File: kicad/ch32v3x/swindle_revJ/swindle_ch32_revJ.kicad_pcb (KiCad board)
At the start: 2 copper layers, 49.8 x 33.3 mm, 64 parts, among them J1 jtag, J2 Conn_01x03_Socket, J2_DFU1 con2, J3 Dbg, J4 USB, J5 Debug port, U1 CH32V303RCT6, U2 LM1117-3.3, U3 3V->VTREF, U4 VTREF->3V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

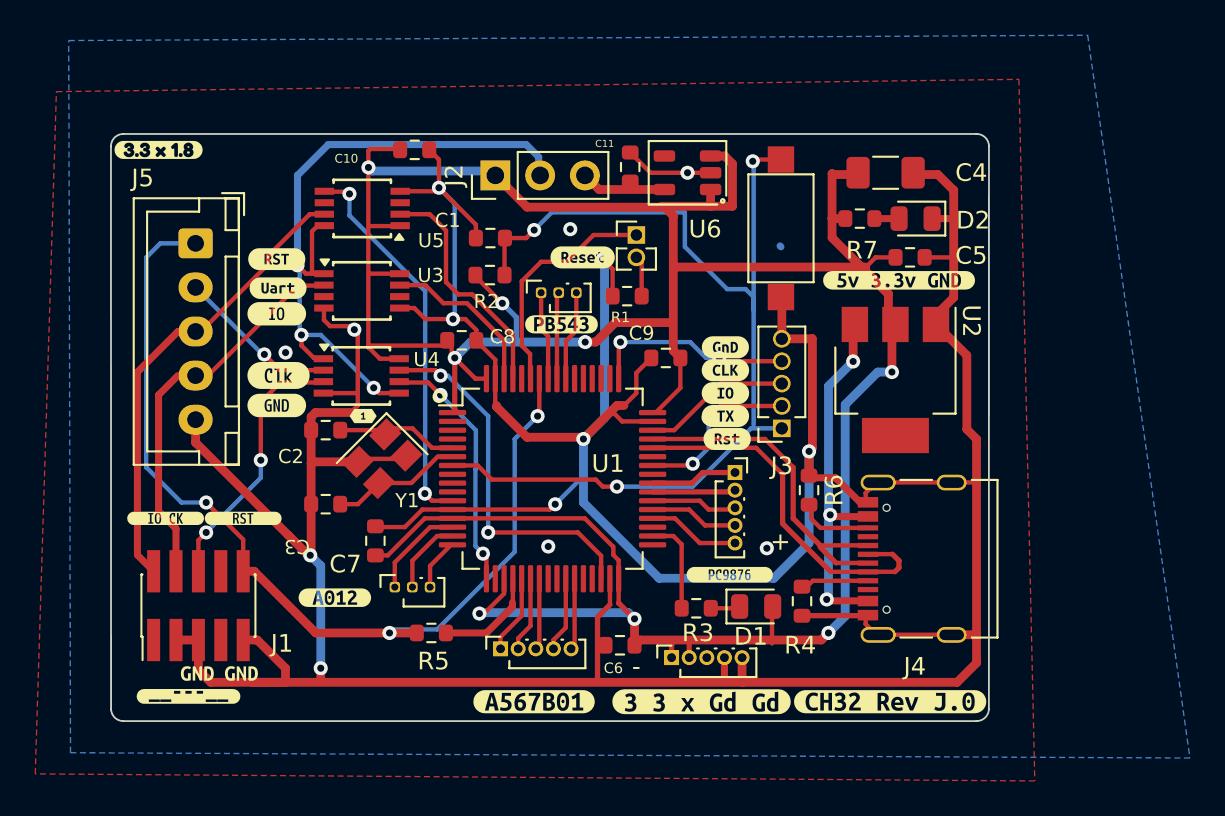
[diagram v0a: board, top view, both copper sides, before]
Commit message: update CH32 pcb
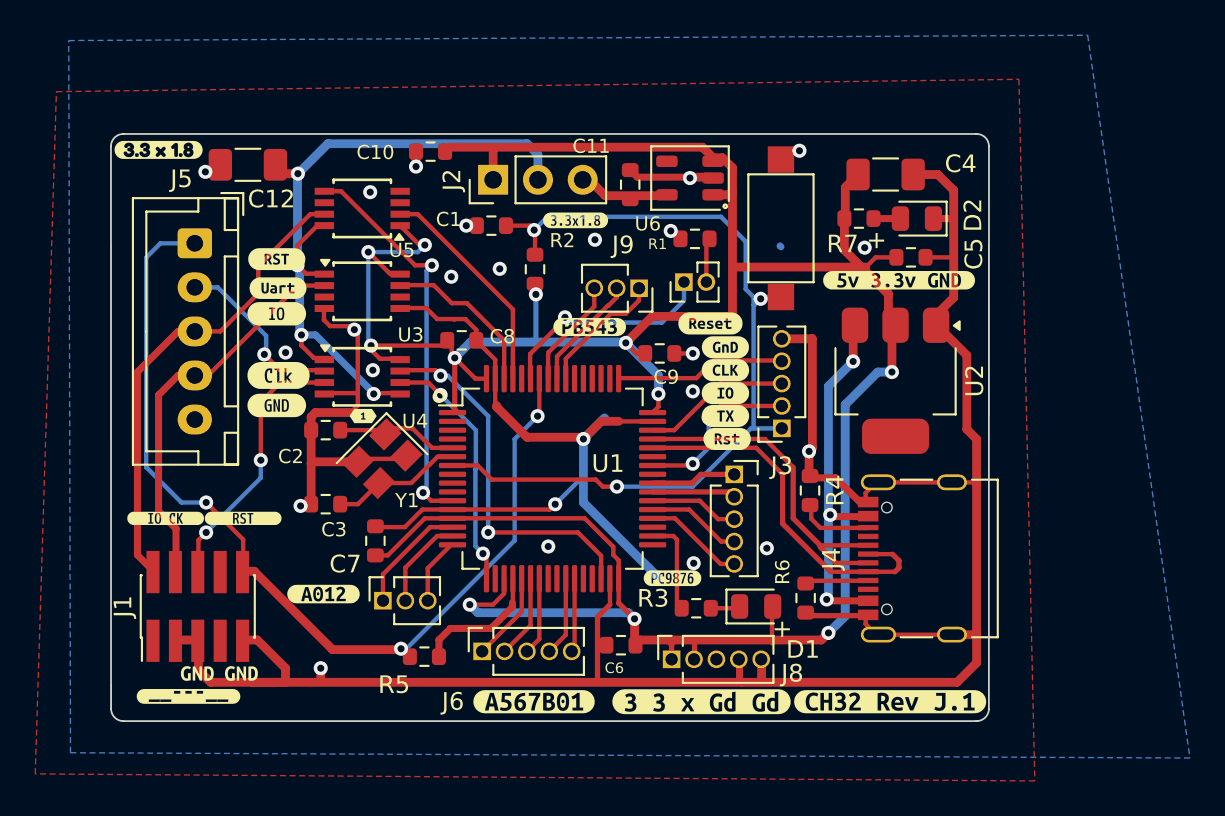
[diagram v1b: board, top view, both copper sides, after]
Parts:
- removed -, PA4567, x2: PinSocket_1x05_P1.00mm_Vertical, Connector_PinSocket_1.00mm:PinSocket_1x05_P1.00mm_Vertical
- removed PB567: PIN1X3, Connector_PinSocket_1.00mm:PinSocket_1x03_P1.00mm_Vertical
- removed kibuzzard-6713D043: G***, kibuzzard-6713D043
- removed kibuzzard-68455F40: G***, kibuzzard-68455F40
- removed x: PinSocket_1x03_P1.00mm_Vertical, Connector_PinSocket_1.00mm:PinSocket_1x03_P1.00mm_Vertical
- added C12: 100u, Capacitor_SMD:C_1206_3216Metric_Pad1.33x1.80mm_HandSolder, F.Cu at (113.3, 68.6)
- added J10: Debug port, Connector_PinSocket_1.27mm:PinSocket_1x05_P1.27mm_Vertical, F.Cu at (140.9, 86.2)
- added J6: Debug port, Connector_PinSocket_1.27mm:PinSocket_1x05_P1.27mm_Vertical, F.Cu at (126.6, 96.2)
- added J7: Conn_01x03_Pin, Connector_PinSocket_1.27mm:PinSocket_1x03_P1.27mm_Vertical, F.Cu at (120.9, 93.4)
- added J8: Debug port, Connector_PinSocket_1.27mm:PinSocket_1x05_P1.27mm_Vertical, F.Cu at (137.3, 96.7)
- added J9: Conn_01x03_Pin, Connector_PinSocket_1.27mm:PinSocket_1x03_P1.27mm_Vertical, F.Cu at (135.5, 75.6)
- added kibuzzard-6869421E: G***, kibuzzard-6869421E, F.Cu at (149.7, 99.1)
- added kibuzzard-68694355: G***, kibuzzard-68694355, F.Cu at (137.4, 92.1)
- added kibuzzard-686943DA: G***, kibuzzard-686943DA, F.Cu at (131.9, 71.8)
- moved kibuzzard-65C1C9D7 8.16 mm to (139.5, 77.6)
- moved R4 6.30 mm to (145.2, 87.1), turned to -90 degrees
- moved R6 6.12 mm to (144.9, 93.2), turned to 90 degrees
- moved R1 5.04 mm to (138.6, 72.8)
- moved J2_DFU1 3.80 mm to (138.0, 75.3), turned to 90 degrees
- moved R2 2.58 mm to (129.6, 74.6), turned to 90 degrees
- moved kibuzzard-67ECD9AB 1.61 mm to (132.7, 77.8)
- moved R5 1.40 mm to (123.3, 96.5)
- moved C11 1.00 mm to (135.0, 69.8)
- moved C10 0.91 mm to (123.6, 67.9), turned to 180 degrees
- moved C1 0.71 mm to (127.1, 72.1)
- moved kibuzzard-67135D9A 0.68 mm to (117.6, 93.0)
- moved C9 0.43 mm to (136.6, 79.3), turned to 0 degrees
- moved U6 0.33 mm to (138.3, 69.4)
- moved J2 0.28 mm to (127.2, 69.5)
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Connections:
- R4 pad 2: Net-(J4-CC1) -> Net-(J4-CC2)
- R6 pad 2: Net-(J4-CC2) -> Net-(J4-CC1)
- U1 pad 14: unconnected-(U1-PA0-Pad14) -> PA0
- U1 pad 15: unconnected-(U1-PA1-Pad15) -> PA1
- U1 pad 16: unconnected-(U1-PA2-Pad16) -> PA2
- U1 pad 21: unconnected-(U1-PA5-Pad21) -> PA5
- U1 pad 22: unconnected-(U1-PA6-Pad22) -> PA6
- U1 pad 23: unconnected-(U1-PA7-Pad23) -> PA7
- U1 pad 26: unconnected-(U1-PB0-Pad26) -> PB0
- U1 pad 27: unconnected-(U1-PB1-Pad27) -> PB1
- U1 pad 36: unconnected-(U1-PB15-Pad36) -> PB15
- U1 pad 37: unconnected-(U1-PC6-Pad37) -> PC6
- U1 pad 38: unconnected-(U1-PC7-Pad38) -> PC7
- U1 pad 39: unconnected-(U1-PC8-Pad39) -> PC8
- U1 pad 40: unconnected-(U1-PC9-Pad40) -> PC9
- U1 pad 55: unconnected-(U1-PB3-Pad55) -> PB3
- U1 pad 56: unconnected-(U1-PB4-Pad56) -> PB4
- U1 pad 57: unconnected-(U1-PB5-Pad57) -> PB5
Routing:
- net GND: track 266.2 -> 200.2 mm, vias 14 -> 24
- net +3.3V: track 178.1 -> 168.5 mm, vias 8 -> 11
- net NRESET: track 57.0 -> 49.1 mm
- net PB3: track 0.00 -> 7.30 mm
- net PB4: track 0.00 -> 6.55 mm
- net PA0: track 0.00 -> 6.55 mm
- net PB5: track 0.00 -> 6.21 mm
- net PB15: track 0.00 -> 5.70 mm
- net unconnected-(U1-PA0-Pad14): track 5.50 -> 0.00 mm
- net PC6: track 0.00 -> 5.38 mm
- net PA1: track 0.00 -> 5.29 mm
- net unconnected-(U1-PB15-Pad36): track 5.25 -> 0.00 mm
- net unconnected-(U1-PB3-Pad55): track 5.12 -> 0.00 mm
- net PC7: track 0.00 -> 5.06 mm
- net PA5: track 0.00 -> 5.05 mm
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
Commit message: kicad: update new wch
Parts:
- removed kibuzzard-686943DA: G***, kibuzzard-686943DA
- moved kibuzzard-6714FCCA 19.6 mm to (127.3, 72.0)
- moved C1 8.13 mm to (135.2, 72.8), turned to 0 degrees
- moved R7 3.00 mm to (148.0, 68.7)
- moved D2 3.00 mm to (151.3, 68.7)
- moved C4 2.74 mm to (150.4, 71.7)
- moved R2 2.57 mm to (131.5, 72.8), turned to 0 degrees
- moved C9 0.86 mm to (137.5, 79.5)
- moved C5 0.58 mm to (151.5, 73.9)
- moved U5 0.52 mm to (119.8, 70.6)
- moved C11 0.40 mm to (135.0, 69.4)
- moved U3 0.22 mm to (119.8, 75.6)
- moved C6 0.16 mm to (134.6, 95.8)
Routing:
- net +3.3V: track 168.5 -> 163.6 mm, vias 11 -> 8
- net NRESET: track 49.1 -> 44.3 mm
- net OUT_SWDIO: track 27.2 -> 28.9 mm
- net IN_FORCE_DFU: track 12.7 -> 14.3 mm, vias 1 -> 0
- net VTREF: track 39.2 -> 40.3 mm
